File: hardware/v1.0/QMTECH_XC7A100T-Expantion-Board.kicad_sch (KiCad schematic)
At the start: 49 parts, among them J1 Micro_SD_Card_Det1, J14 USB_C_Receptacle_USB2.0_16P, J15 Conn_02x06_Odd_Even, J16 Conn_02x06_Odd_Even, J2 Conn_01x34, J3 USB_C_Receptacle_USB2.0_16P, J4 Conn_01x34, Q1 AON6411, U14 HUSB238, U15 CH340C

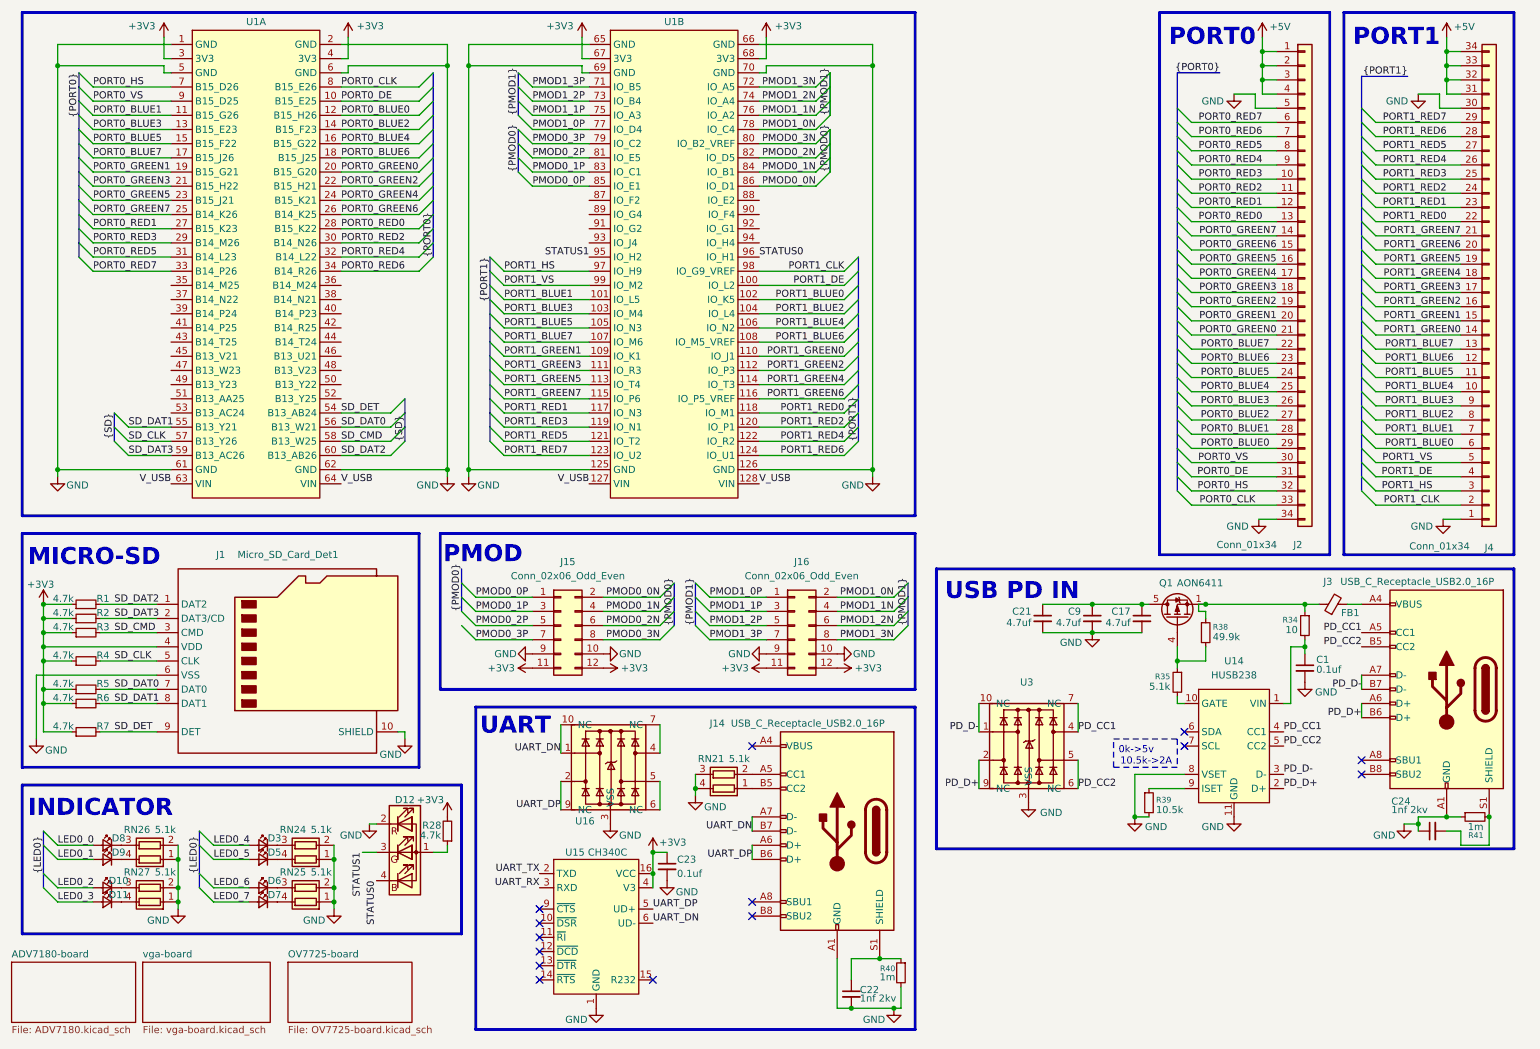
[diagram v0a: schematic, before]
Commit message: did PORT0 routing
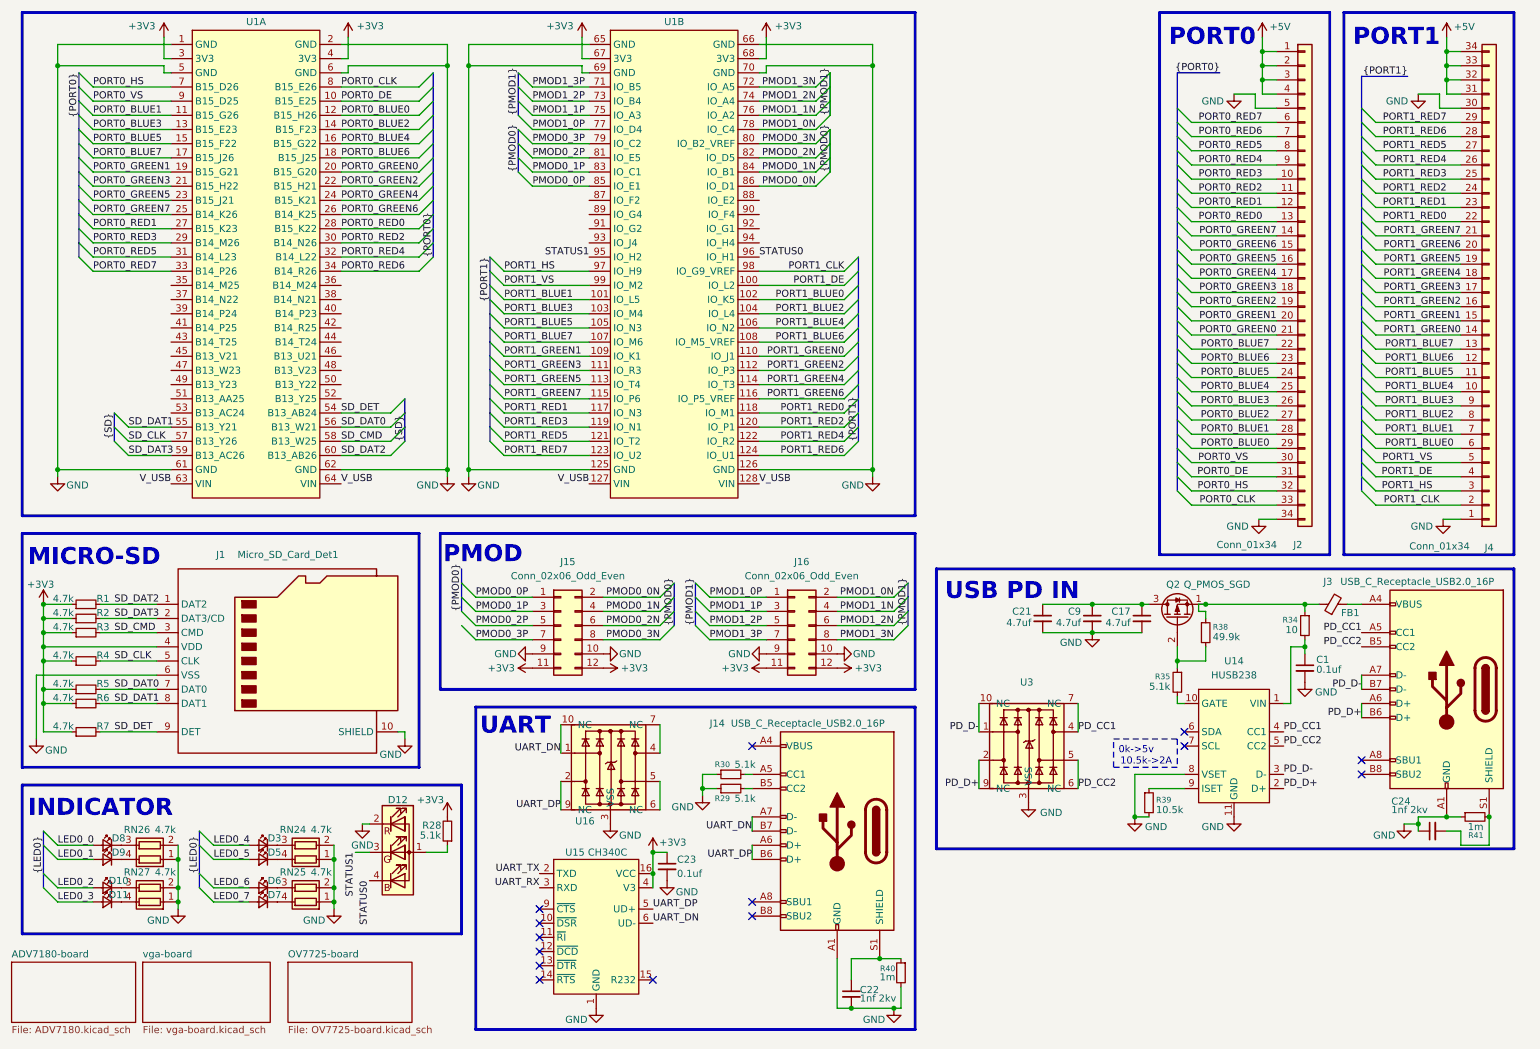
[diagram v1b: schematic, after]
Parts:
- removed Q1: AON6411, Package_DFN_QFN:AO_DFN-8-1EP_5.55x5.2mm_P1.27mm_EP4.12x4.6mm, symbol Transistor_FET:AON6411
- removed RN21: 5.1k, symbol Device:R_Pack02
- added Q2: Q_PMOS_SGD, Package_DFN_QFN:DFN-8-1EP_3x3mm_P0.5mm_EP1.7x2.4mm, symbol Transistor_FET:Q_PMOS_SGD
- added R29, R30: 5.1k, Resistor_SMD:R_0603_1608Metric, symbol Device:R_Small
- R28: value 4.7k -> 5.1k
- RN24, RN25, RN26, RN27: value 5.1k -> 4.7k; footprint (none) -> Resistor_SMD:R_Array_Convex_2x0603
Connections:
- net GND: now also R29.1, R30.1
- net at J14.B5 (CC2): now also R29.2
- net at J14.A5 (CC1): now also R30.2
- net at C17.1, C21.1, C9.1: now also Q2.3 (D)
- net at FB1.1, R34.1, R38.1: now also Q2.1 (S)
- net at R35.1, R38.2: now also Q2.2 (G)
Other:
- moved on the sheet: D12

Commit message: changes
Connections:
- net V_USB is gone; now on net +5V: U1.127 (VIN), U1.128 (VIN), U1.63 (VIN), U1.64 (VIN)
- net +5V: now also C17.1, C21.1, C9.1, Q2.3 (D)
- net PMOD0_0N: now also U1.85 (IO_E1); no longer U1.86 (IO_D1)
- net PMOD0_0P: now also U1.86 (IO_D1); no longer U1.85 (IO_E1)
- net PMOD0_1N: now also U1.83 (IO_C1); no longer U1.84 (IO_B1)
- net PMOD0_1P: now also U1.84 (IO_B1); no longer U1.83 (IO_C1)
- net PMOD0_2N: now also U1.81 (IO_E5); no longer U1.82 (IO_D5)
- net PMOD0_2P: now also U1.82 (IO_D5); no longer U1.81 (IO_E5)
- net PMOD0_3N: now also U1.79 (IO_C2); no longer U1.80 (IO_B2_VREF)
- net PMOD0_3P: now also U1.80 (IO_B2_VREF); no longer U1.79 (IO_C2)
- net PMOD1_0N: now also U1.77 (IO_D4); no longer U1.78 (IO_C4)
- net PMOD1_0P: now also U1.78 (IO_C4); no longer U1.77 (IO_D4)
- net PMOD1_1N: now also U1.75 (IO_A3); no longer U1.76 (IO_A2)
- net PMOD1_1P: now also U1.76 (IO_A2); no longer U1.75 (IO_A3)
- net PMOD1_2N: now also U1.73 (IO_B4); no longer U1.74 (IO_A4)
- net PMOD1_2P: now also U1.74 (IO_A4); no longer U1.73 (IO_B4)
- net PMOD1_3N: now also U1.71 (IO_B5); no longer U1.72 (IO_A5)
- net PMOD1_3P: now also U1.72 (IO_A5); no longer U1.71 (IO_B5)
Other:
- note added: "LEDS"
- note removed: "INDICATOR"

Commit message: finished mainboard + progress on peripherals
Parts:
- removed C22, C24: 1nf 2kv, symbol Device:C_Small
- removed FB1: ~, symbol Device:FerriteBead_Small
- removed Q2: Q_PMOS_SGD, Package_DFN_QFN:DFN-8-1EP_3x3mm_P0.5mm_EP1.7x2.4mm, symbol Transistor_FET:Q_PMOS_SGD
- removed R40, R41: 1m, symbol Device:R_Small
- added D13: SP1003, symbol Device:D_Small_Filled
- added Q1: Si7121DN, Package_SO:Vishay_PowerPAK_1212-8_Single, symbol mylib:Si7121DN
- added TH1: 1812L200THPR, Resistor_SMD:R_1812_4532Metric, symbol Device:Thermistor_PTC
- C1, C17, C21, C23, C9: footprint (none) -> Capacitor_SMD:C_0603_1608Metric
- R34, R35, R38, R39: footprint (none) -> Resistor_SMD:R_0603_1608Metric
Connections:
- net +5V: now also Q1.5 (D)
- net GND: now also J14.S1 (SHIELD), J3.S1 (SHIELD), D13.2 (A)
- net LED0_0: now also U1.90 (IO_F4)
- net LED0_1: now also U1.89 (IO_G4)
- net LED0_2: now also U1.87 (IO_F2)
- net LED0_3: now also U1.88 (IO_E2)
- net LED0_4: now also U1.92 (IO_G1)
- net LED0_5: now also U1.91 (IO_G2)
- net LED0_6: now also U1.94 (IO_H4)
- net LED0_7: now also U1.93 (IO_J4)
- net PD_D+: now also U3.1, U3.10 (NC); no longer U3.2, U3.9 (NC)
- net PD_D-: now also U3.2, U3.9 (NC); no longer U3.1, U3.10 (NC)
- net PMOD0_0N: now also U1.86 (IO_D1); no longer U1.85 (IO_E1)
- net PMOD0_0P: now also U1.85 (IO_E1); no longer U1.86 (IO_D1)
- net PMOD0_1N: now also U1.84 (IO_B1); no longer U1.83 (IO_C1)
- net PMOD0_1P: now also U1.83 (IO_C1); no longer U1.84 (IO_B1)
- net PMOD0_2N: now also U1.82 (IO_D5); no longer U1.81 (IO_E5)
- net PMOD0_2P: now also U1.81 (IO_E5); no longer U1.82 (IO_D5)
- net PMOD0_3N: now also U1.80 (IO_B2_VREF); no longer U1.79 (IO_C2)
- net PMOD0_3P: now also U1.79 (IO_C2); no longer U1.80 (IO_B2_VREF)
- net PMOD1_0N: now also U1.78 (IO_C4); no longer U1.77 (IO_D4)
- net PMOD1_0P: now also U1.77 (IO_D4); no longer U1.78 (IO_C4)
- net PMOD1_1N: now also U1.76 (IO_A2); no longer U1.75 (IO_A3)
- net PMOD1_1P: now also U1.75 (IO_A3); no longer U1.76 (IO_A2)
- net PMOD1_2N: now also U1.74 (IO_A4); no longer U1.73 (IO_B4)
- net PMOD1_2P: now also U1.73 (IO_B4); no longer U1.74 (IO_A4)
- net PMOD1_3N: now also U1.72 (IO_A5); no longer U1.71 (IO_B5)
- net PMOD1_3P: now also U1.71 (IO_B5); no longer U1.72 (IO_A5)
- net UART_RX: now also U1.51 (B13_AA25)
- net UART_TX: now also U1.53 (B13_AC24)
- net at R34.1, R38.1: now also D13.1 (K), Q1.1 (S), Q1.2 (S), Q1.3 (S), TH1.1
- net at J3.A4 (VBUS), J3.A9 (VBUS), J3.B4 (VBUS)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: now also TH1.2
- net at R35.1, R38.2: now also Q1.4 (G)
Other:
- moved on the sheet: C1, R34, R35, U14
